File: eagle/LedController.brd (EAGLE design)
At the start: 64.8 x 34.3 mm, 32 parts, among them IC1 MCP601R, IC3 7805, Q1 16MHz, Q5 PMV20EN, X1 2510-, X2 MKDSN1,5/4-5,08

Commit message: Change voltage regulator to DPAK variant
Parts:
- removed IC3: 7805, v-reg:78XXS
- added U$6: L78M05ABDT-TR, LedController:DPAK
- moved X1 4.45 mm to (40.0, 25.4)
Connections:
- net +12V: now also U$6.1; no longer IC3.IN
- net +5V: now also U$6.3; no longer IC3.OUT
- net GND: now also U$6.4; no longer IC3.GND
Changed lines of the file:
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@@
 <element name="C1" library="rcl" package="C0805" value="22pF" x="31.75" y="7.62"/>
 <element name="C2" library="rcl" package="C0805" value="22pF" x="26.67" y="7.62" rot="R180"/>
-<element name="IC3" library="v-reg" package="78XXS" value="7805" x="24.765" y="26.67" rot="R270"/>
 <element name="C7" library="rcl" package="C0805" value="100nF" x="16.51" y="27.94" rot="R270"/>
 <element name="C9" library="rcl" package="C0805" value="100nF" x="19.685" y="5.715" rot="R180"/>
@@
 <element name="C10" library="rcl" package="C0805" value="100nF" x="19.05" y="25.4" rot="R90"/>
 <element name="C15" library="rcl" package="E2-5" value="4.7uF" x="14.859" y="3.81" rot="R180"/>
-<element name="X1" library="con-3m" package="PAK100/2500-10" value="2510-" x="35.56" y="25.4">
-<attribute name="OC_NEWARK" value="46F4725" x="35.56" y="25.4" size="1.778" layer="27" display="off"/>
-<attribute name="OC_FARNELL" value="9838244" x="35.56" y="25.4" size="1.778" layer="27" display="off"/>
-<attribute name="MF" value="3M" x="35.56" y="25.4" size="1.778" layer="27" display="off"/>
-<attribute name="MPN" value="2510-6002UB" x="35.56" y="25.4" size="1.778" layer="27" display="off"/>
+<element name="X1" library="con-3m" package="PAK100/2500-10" value="2510-" x="40.005" y="25.4">
+<attribute name="OC_NEWARK" value="46F4725" x="40.005" y="25.4" size="1.778" layer="27" display="off"/>
+<attribute name="OC_FARNELL" value="9838244" x="40.005" y="25.4" size="1.778" layer="27" display="off"/>
+<attribute name="MF" value="3M" x="40.005" y="25.4" size="1.778" layer="27" display="off"/>
+<attribute name="MPN" value="2510-6002UB" x="40.005" y="25.4" size="1.778" layer="27" display="off"/>
 </element>
 <element name="C4" library="rcl" package="E2-5" value="100uF" x="12.7" y="25.4" rot="R270"/>
@@
 <element name="C8" library="rcl" package="C0805" value="100nF" x="19.685" y="8.255"/>
 <element name="U$5" library="LedController" package="TSOP75236" value="TSOP75236" x="6.35" y="4.445" rot="R180"/>
+<element name="U$6" library="LedController" package="DPAK" value="L78M05ABDT-TR" x="24.13" y="27.94"/>
 </elements>
 <signals>
@@
 <contactref element="X1" pad="10"/>
 <contactref element="X1" pad="4"/>
-<contactref element="IC3" pad="GND"/>
 <contactref element="C7" pad="2"/>
 <contactref element="C10" pad="2"/>
@@
 <contactref element="U$5" pad="P$4"/>
 <contactref element="U$5" pad="P$1"/>
-<wire x1="38.1" y1="26.67" x2="40.64" y2="26.67" width="0" layer="19" extent="1-1"/>
-<wire x1="35.56" y1="26.67" x2="38.1" y2="26.67" width="0" layer="19" extent="1-1"/>
-<wire x1="33.02" y1="26.67" x2="35.56" y2="26.67" width="0" layer="19" extent="1-1"/>
-<wire x1="36.51" y1="32.385" x2="35.56" y2="26.67" width="0" layer="19" extent="1-1"/>
-<wire x1="26.27" y1="18.8976" x2="33.02" y2="26.67" width="0" layer="19" extent="1-1"/>
+<contactref element="U$6" pad="4"/>
+<wire x1="42.545" y1="26.67" x2="45.085" y2="26.67" width="0" layer="19" extent="1-1"/>
+<wire x1="40.005" y1="26.67" x2="42.545" y2="26.67" width="0" layer="19" extent="1-1"/>
+<wire x1="37.465" y1="26.67" x2="40.005" y2="26.67" width="0" layer="19" extent="1-1"/>
+<wire x1="36.51" y1="32.385" x2="40.005" y2="26.67" width="0" layer="19" extent="1-1"/>
+<wire x1="26.27" y1="18.8976" x2="37.465" y2="26.67" width="0" layer="19" extent="1-1"/>
 <wire x1="27.07" y1="10.3124" x2="26.27" y2="18.8976" width="0" layer="19" extent="1-1"/>
 <wire x1="25.47" y1="10.3124" x2="27.07" y2="10.3124" width="0" layer="19" extent="1-1"/>
 <wire x1="27.62" y1="7.62" x2="27.07" y2="10.3124" width="0" layer="19" extent="1-1"/>
 <wire x1="30.8" y1="7.62" x2="27.62" y2="7.62" width="0" layer="19" extent="1-1"/>
-<wire x1="22.225" y1="26.67" x2="26.27" y2="18.8976" width="0" layer="19" extent="1-1"/>
-<wire x1="19.05" y1="26.35" x2="22.225" y2="26.67" width="0" layer="19" extent="1-1"/>
+<wire x1="19.05" y1="26.35" x2="26.27" y2="18.8976" width="0" layer="19" extent="1-1"/>
 <wire x1="16.51" y1="26.99" x2="19.05" y2="26.35" width="0" layer="19" extent="1-1"/>
 <wire x1="12.7" y1="24.384" x2="16.51" y2="26.99" width="0" layer="19" extent="1-1"/>
@@
 <wire x1="43.35" y1="4.765" x2="43.35" y2="9.21" width="0" layer="19" extent="1-1"/>
 <wire x1="43.35" y1="14.29" x2="43.35" y2="9.21" width="0" layer="19" extent="1-1"/>
+<wire x1="13.843" y1="3.81" x2="25.47" y2="10.3124" width="0" layer="19" extent="1-1"/>
+<wire x1="8.255" y1="5.245" x2="13.843" y2="3.81" width="0" layer="19" extent="1-1"/>
+<wire x1="4.445" y1="5.245" x2="8.255" y2="5.245" width="0" layer="19" extent="1-1"/>
+<wire x1="24.13" y1="31.2928" x2="4.445" y2="5.245" width="0" layer="19" extent="1-1"/>
 <wire x1="14.569" y1="40.96" x2="16.51" y2="26.99" width="0" layer="19" extent="1-1"/>
 <wire x1="18.73" y1="45.72" x2="14.569" y2="40.96" width="0" layer="19" extent="1-1"/>
 <wire x1="22.225" y1="40.955" x2="18.73" y2="45.72" width="0" layer="19" extent="1-1"/>
-<wire x1="13.843" y1="3.81" x2="9.06" y2="19.37" width="0" layer="19" extent="1-1"/>
-<wire x1="8.255" y1="5.245" x2="13.843" y2="3.81" width="0" layer="19" extent="1-1"/>
-<wire x1="4.445" y1="5.245" x2="8.255" y2="5.245" width="0" layer="19" extent="1-1"/>
 </signal>
 <signal name="N$3">
@@
 <contactref element="X1" pad="1"/>
 <contactref element="U$4" pad="15"/>
-<wire x1="30.9626" y1="16.605" x2="30.48" y2="24.13" width="0" layer="19" extent="1-1"/>
+<wire x1="30.9626" y1="16.605" x2="34.925" y2="24.13" width="0" layer="19" extent="1-1"/>
 </signal>
 <signal name="ISP_CLK">
 <contactref element="X1" pad="7"/>
 <contactref element="U$4" pad="17"/>
-<wire x1="29.47" y1="18.8976" x2="38.1" y2="24.13" width="0" layer="19" extent="1-1"/>
+<wire x1="29.47" y1="18.8976" x2="42.545" y2="24.13" width="0" layer="19" extent="1-1"/>
 </signal>
 <signal name="ISP_MISO">
 <contactref element="X1" pad="9"/>
 <contactref element="U$4" pad="16"/>
-<wire x1="30.9626" y1="17.405" x2="40.64" y2="24.13" width="0" layer="19" extent="1-1"/>
+<wire x1="30.9626" y1="17.405" x2="45.085" y2="24.13" width="0" layer="19" extent="1-1"/>
 </signal>
 <signal name="IR">
@@
 <contactref element="PS" pad="1"/>
 <contactref element="Q5" pad="1"/>
-<contactref element="IC3" pad="IN"/>
 <contactref element="C7" pad="1"/>
 <contactref element="C4" pad="+"/>
-<wire x1="22.225" y1="29.21" x2="59.665" y2="20.9339" width="0" layer="19" extent="1-1"/>
-<wire x1="16.51" y1="28.89" x2="22.225" y2="29.21" width="0" layer="19" extent="1-1"/>
+<contactref element="U$6" pad="1"/>
+<wire x1="16.51" y1="28.89" x2="59.665" y2="20.9339" width="0" layer="19" extent="1-1"/>
 <wire x1="12.7" y1="26.416" x2="16.51" y2="28.89" width="0" layer="19" extent="1-1"/>
 <wire x1="9.06" y1="21.27" x2="12.7" y2="26.416" width="0" layer="19" extent="1-1"/>
 <wire x1="5.105" y1="29.2311" x2="12.7" y2="26.416" width="0" layer="19" extent="1-1"/>
+<wire x1="21.8694" y1="23.0124" x2="9.06" y2="21.27" width="0" layer="19" extent="1-1"/>
 </signal>
 <signal name="+5V">
 <contactref element="X1" pad="2"/>
-<contactref element="IC3" pad="OUT"/>
 <contactref element="C10" pad="1"/>
 <contactref element="R1" pad="1"/>
@@
 <contactref element="U$4" pad="4"/>
 <contactref element="U$4" pad="6"/>
-<wire x1="30.48" y1="26.67" x2="29.53" y2="32.385" width="0" layer="19" extent="1-1"/>
-<wire x1="22.225" y1="24.13" x2="30.48" y2="26.67" width="0" layer="19" extent="1-1"/>
-<wire x1="19.05" y1="24.45" x2="22.225" y2="24.13" width="0" layer="19" extent="1-1"/>
+<contactref element="U$6" pad="3"/>
+<wire x1="34.925" y1="26.67" x2="29.53" y2="32.385" width="0" layer="19" extent="1-1"/>
+<wire x1="19.05" y1="24.45" x2="34.925" y2="26.67" width="0" layer="19" extent="1-1"/>
 <wire x1="15.875" y1="22.54" x2="19.05" y2="24.45" width="0" layer="19" extent="1-1"/>
 <wire x1="14.285" y1="15.24" x2="15.875" y2="22.54" width="0" layer="19" extent="1-1"/>
@@
 <wire x1="12.385" y1="45.72" x2="17.181" y2="41.91" width="0" layer="19" extent="1-1"/>
 <wire x1="9.525" y1="42.86" x2="12.385" y2="45.72" width="0" layer="19" extent="1-1"/>
+<wire x1="26.3398" y1="23.0124" x2="14.285" y2="15.24" width="0" layer="19" extent="1-1"/>
 </signal>
 <signal name="ISP_RESET">
@@
 <contactref element="R1" pad="2"/>
 <contactref element="U$4" pad="29"/>
-<wire x1="22.3774" y1="14.205" x2="35.56" y2="24.13" width="0" layer="19" extent="1-1"/>
+<wire x1="22.3774" y1="14.205" x2="40.005" y2="24.13" width="0" layer="19" extent="1-1"/>
 <wire x1="15.875" y1="20.64" x2="22.3774" y2="14.205" width="0" layer="19" extent="1-1"/>
 </signal>

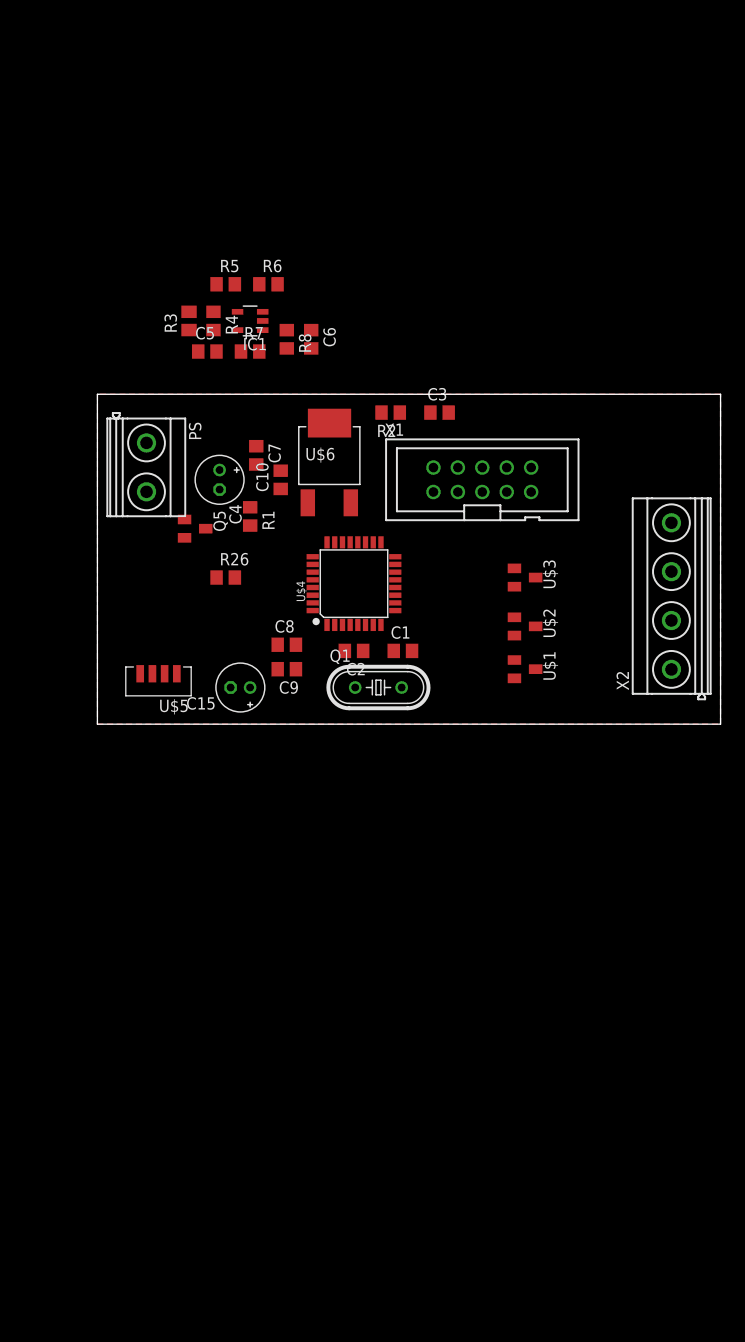
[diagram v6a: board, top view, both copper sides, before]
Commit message: Add DC Barrel Jack
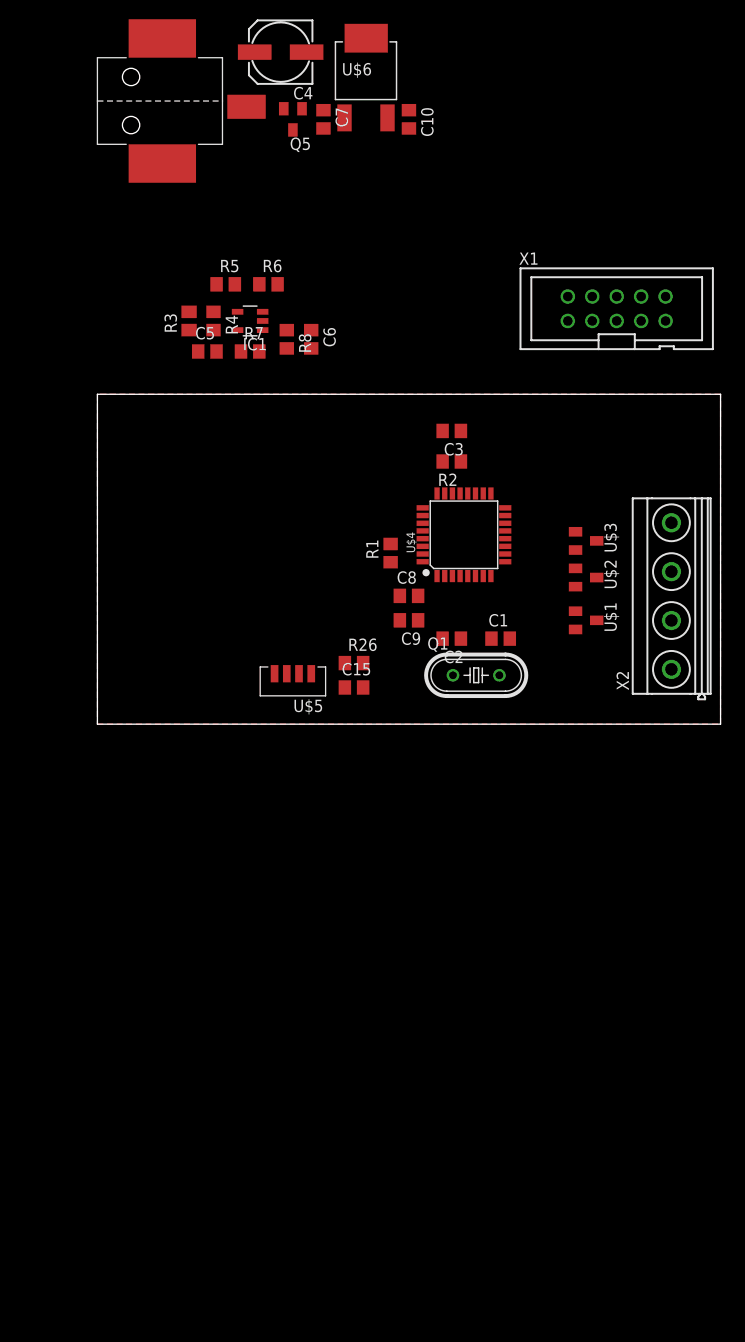
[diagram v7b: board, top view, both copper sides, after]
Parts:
- removed PS: MKDSN1,5/2-5,08, con-phoenix-508:MKDSN1,5/2-5,08
- added U$7: DCJACK, LedController:DCJACK
- C15: value 4.7uF -> 1uF; device rcl:E2-5 -> rcl:C0805
- C4: device rcl:E2-5 -> rcl:153CLV-0605
- C7: value 100nF -> 330nF
- moved C4 44.9 mm to (19.1, 69.8), turned to 180 degrees
- moved Q5 43.7 mm to (20.3, 62.9), turned to 180 degrees
- moved U$6 40.2 mm to (27.9, 67.9)
- moved C10 39.8 mm to (32.4, 62.9), turned to 270 degrees
- moved C7 35.6 mm to (23.5, 62.9)
- moved X1 22.6 mm to (54.0, 43.2)
- moved R26 16.0 mm to (26.7, 6.35)
- moved R1 15.1 mm to (30.5, 17.8), turned to 90 degrees
- moved U$5 14.0 mm to (20.3, 4.45)
- moved C8 13.7 mm to (32.4, 13.3)
- moved C9 13.7 mm to (32.4, 10.8)
- moved U$4 12.5 mm to (38.1, 19.7)
- moved C15 11.8 mm to (26.7, 3.81), turned to 0 degrees
- moved C1 10.2 mm to (41.9, 8.89)
- moved C2 10.2 mm to (36.8, 8.89)
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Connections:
- net +12V: now also U$7.1; no longer PS.1
- net GND: now also C15.2; no longer C15.-
- net N$63: now also C15.1; no longer C15.+
- net N$8: now also U$7.2; no longer PS.2

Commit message: Cosmetic Changes in Board Schematic
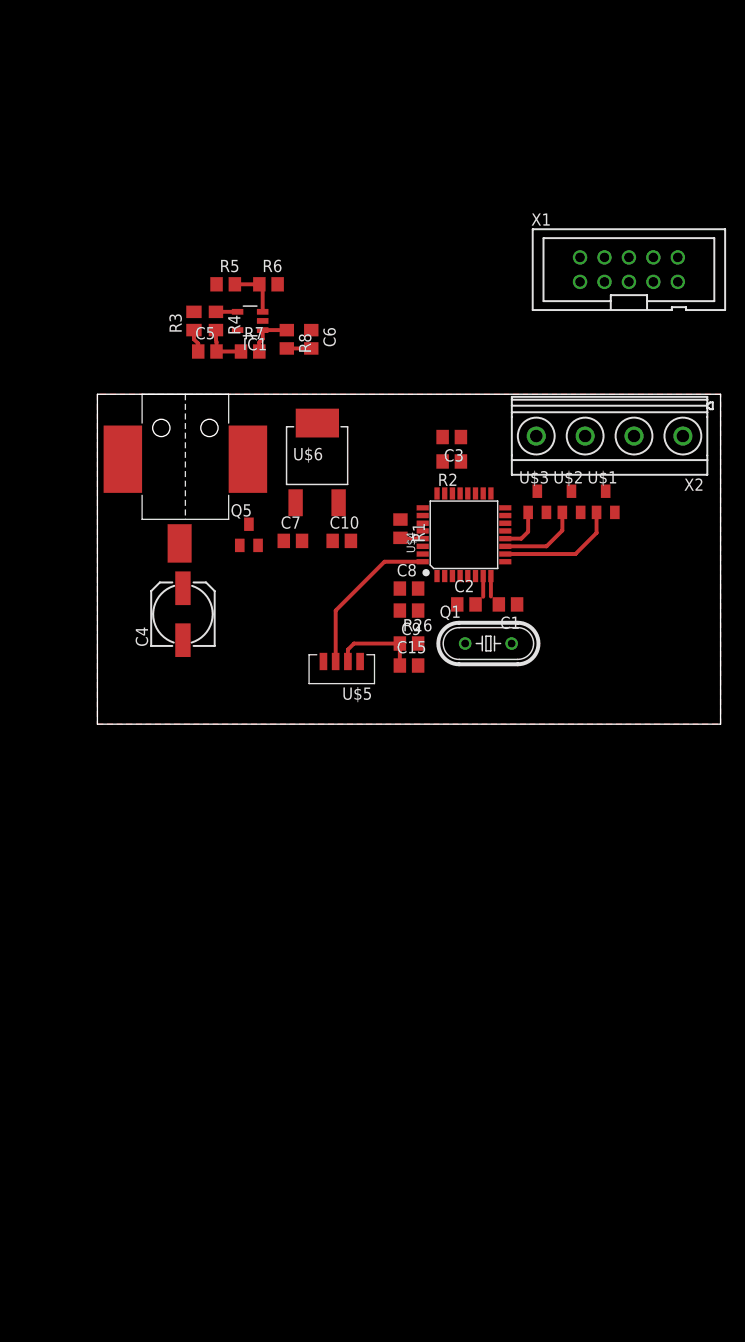
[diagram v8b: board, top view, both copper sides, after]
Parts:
- moved C4 59.3 mm to (8.89, 11.4), turned to 90 degrees
- moved C10 44.4 mm to (25.4, 19.1), turned to 0 degrees
- moved C7 43.9 mm to (20.3, 19.1), turned to 0 degrees
- moved Q5 43.4 mm to (15.7, 19.7), turned to 0 degrees
- moved U$6 40.3 mm to (22.9, 27.9)
- moved U$7 31.8 mm to (9.14, 34.3), turned to 270 degrees
- moved X2 17.9 mm to (53.2, 30.0), turned to 180 degrees
- moved U$1 12.5 mm to (52.8, 23.1), turned to 0 degrees
- moved U$2 8.02 mm to (49.3, 23.1), turned to 0 degrees
- moved U$3 6.51 mm to (45.7, 23.1), turned to 0 degrees
- moved C15 6.16 mm to (32.4, 6.10)
- moved R26 6.07 mm to (32.4, 8.38)
- moved U$5 5.24 mm to (25.4, 5.71)
- moved X1 4.26 mm to (55.2, 47.2)
- moved C2 3.87 mm to (38.4, 12.4), turned to 0 degrees
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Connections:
- new net N$2: C1.2, Q1.2
- net N$13: no longer C1.2, Q1.2
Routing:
- net IR: track 0.00 -> 16.4 mm
- net PWM_R: track 0.00 -> 12.5 mm
- net N$63: track 0.00 -> 9.18 mm
- net PWM_G: track 0.00 -> 8.50 mm
- net N$11: track 0.00 -> 5.55 mm
- net N$12: track 0.00 -> 4.88 mm
- net N$9: track 0.00 -> 4.78 mm
- net PWM_B: track 0.00 -> 4.69 mm
- net ADC: track 0.00 -> 2.54 mm
- net N$1: track 0.00 -> 2.41 mm
- net ISP_RESET: track 0.00 -> 2.35 mm
- net N$10: track 0.00 -> 2.25 mm
- net N$14: track 0.00 -> 2.15 mm
- net N$13: track 0.00 -> 2.12 mm
